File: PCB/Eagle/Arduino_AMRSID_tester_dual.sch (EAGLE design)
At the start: 21 parts

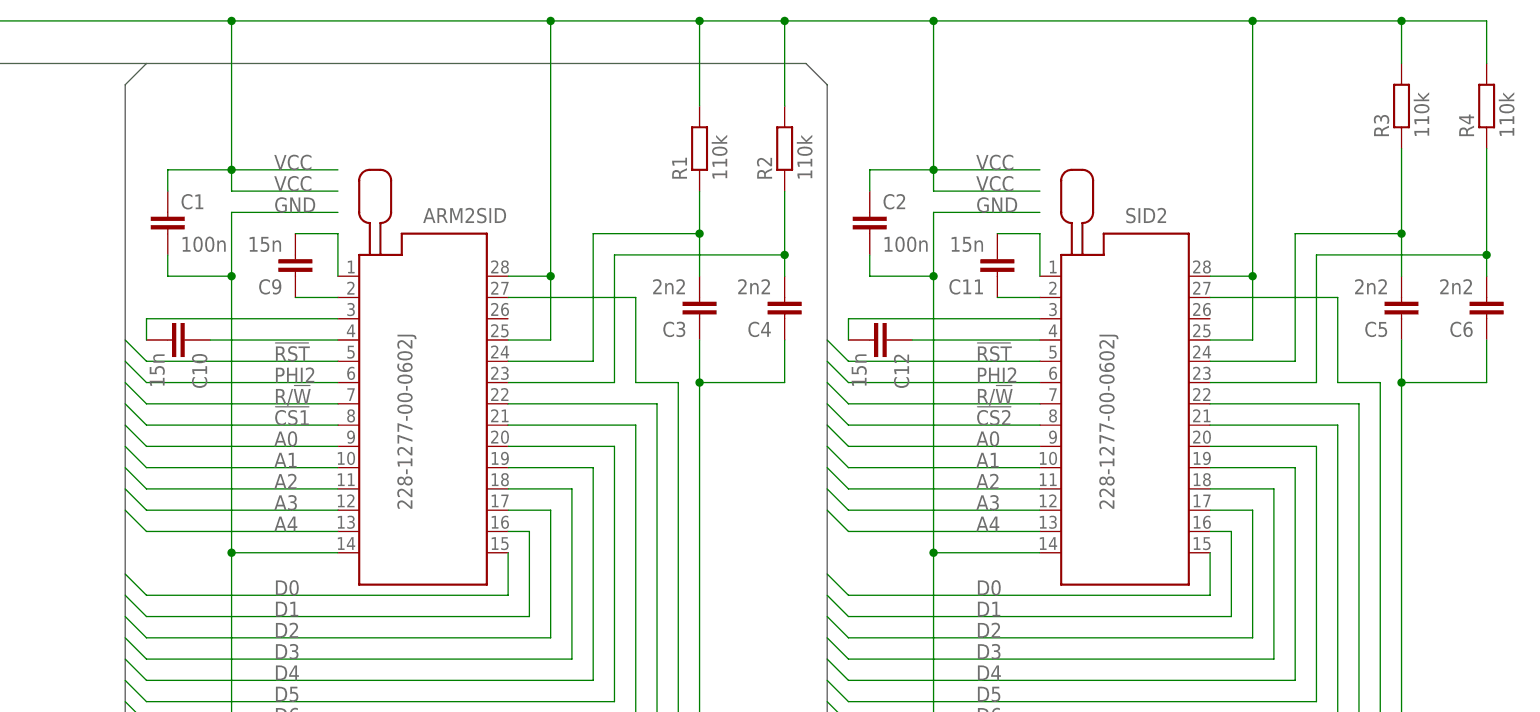
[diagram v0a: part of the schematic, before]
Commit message: Schematic update for better readability
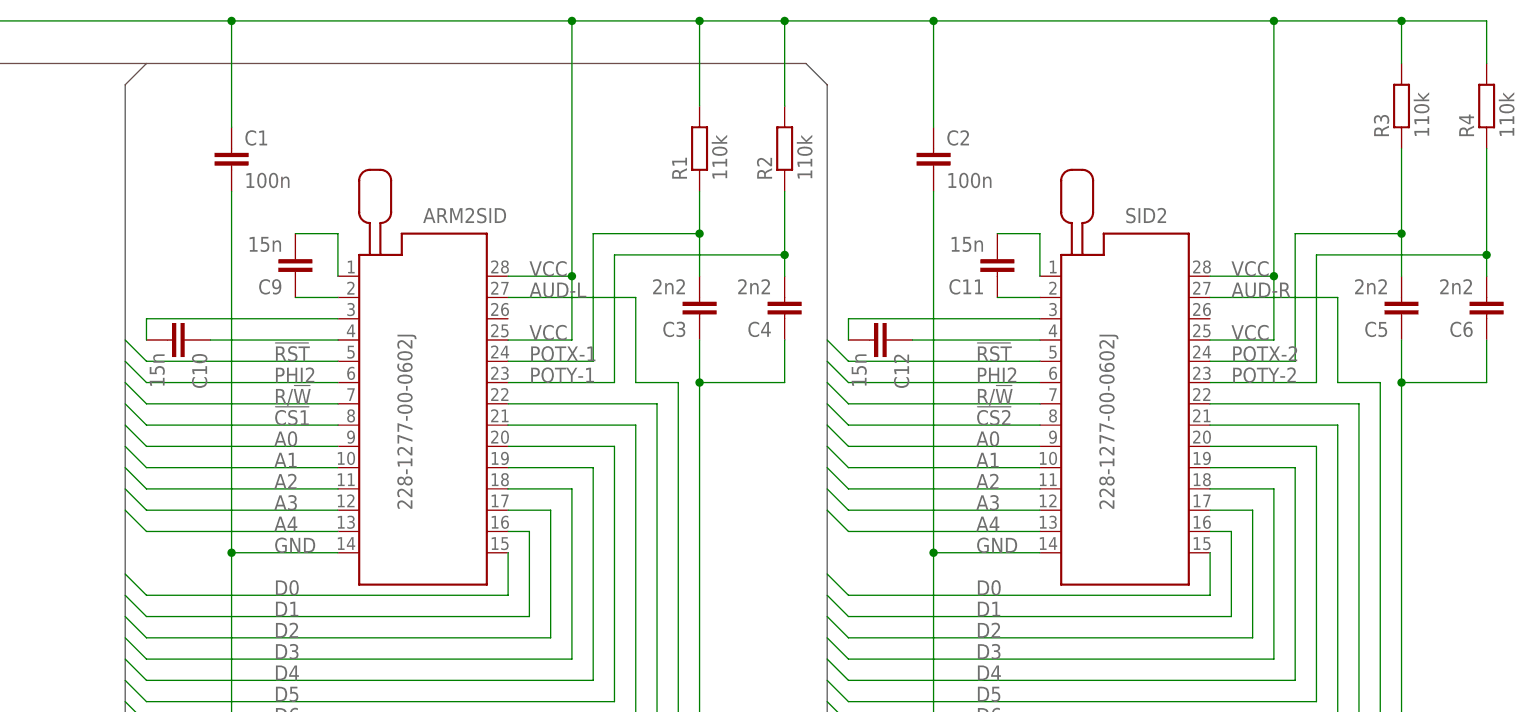
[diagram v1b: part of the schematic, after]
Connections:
- net N$3 renamed AUD-R
- net N$5 renamed POTX-1
- net N$6 renamed POTY-1
- net N$7 renamed AUD-L
- net N$8 renamed POTX-2
- net N$9 renamed POTY-2
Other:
- moved on the sheet: C1, C2

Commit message: SCH and PCB update
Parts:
- C10, C11, C12, C9: value 15n -> n.c.
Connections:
- net POTX-1 renamed POTX-L
- net POTX-2 renamed POTX-R
- net POTY-1 renamed POTY-L
- net POTY-2 renamed POTY-R
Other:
- note added: "VDD"
- moved on the sheet: ARM2SID, AUDIO1, B1, C1, C10, C11, C12, C2, C3, C4, C5, C6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
